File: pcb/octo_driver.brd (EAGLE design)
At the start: 34.3 x 46.2 mm, 22 parts, among them U1 LP2985-10DBVT

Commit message: fixed lots of warnings, general cleanup
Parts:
- removed TP1: PTR1B2,54, testpad:B2,54
- C3: value (none) -> 1uF
- JP1, SV1: value (none) -> (none)
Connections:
- new net N$2: C1.1, U1.5
- net GND: now also H2.B2,8, H3.B2,8; no longer TP1.TP
- net VCC: no longer C1.1, U1.5
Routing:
- net VCC: track 68.4 -> 64.6 mm
- net N$2: track 0.00 -> 2.25 mm
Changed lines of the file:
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@@
 <attribute name="NAME" x="59.182" y="46.355" size="1.27" layer="25" rot="R270"/>
 </element>
-<element name="JP1" library="SparkFun-Connectors" package="1X02" value="" x="39.878" y="66.548" smashed="yes" rot="R270">
+<element name="JP1" library="SparkFun-Connectors" package="1X02" value=" " x="39.878" y="66.548" smashed="yes" rot="R270">
 <attribute name="VALUE" x="36.703" y="67.818" size="1.27" layer="27" rot="R270"/>
 </element>
@@
 <element name="H2" library="holes" package="2,8-PAD" value="MOUNT-PAD-ROUND2.8" x="40.666" y="71.12"/>
 <element name="H3" library="holes" package="2,8-PAD" value="MOUNT-PAD-ROUND2.8" x="66.294" y="71.12"/>
-<element name="C3" library="rcl" package="C0805" value="" x="55.88" y="33.782" smashed="yes">
-<attribute name="NAME" x="58.166" y="33.274" size="1.27" layer="25"/>
-<attribute name="VALUE" x="54.61" y="31.242" size="1.27" layer="27"/>
-</element>
-<element name="SV1" library="penrose-con-lstb" package="MA09-1" value="" x="39.878" y="50.546" smashed="yes" rot="R90">
+<element name="C3" library="rcl" package="C0805" value="1uF" x="55.88" y="33.782" smashed="yes">
+<attribute name="VALUE" x="57.658" y="33.274" size="1.27" layer="27"/>
+</element>
+<element name="SV1" library="penrose-con-lstb" package="MA09-1" value=" " x="39.878" y="50.546" smashed="yes" rot="R90">
 <attribute name="OC_NEWARK" value="unknown" x="39.878" y="50.546" size="1.778" layer="27" rot="R90" display="off"/>
 <attribute name="MPN" value="" x="39.878" y="50.546" size="1.778" layer="27" rot="R90" display="off"/>
@@
 <element name="C2" library="rcl" package="C0805" value="1uF" x="43.18" y="66.548" smashed="yes">
 <attribute name="NAME" x="41.91" y="67.818" size="1.27" layer="25" font="vector" ratio="20" display="off"/>
-<attribute name="VALUE" x="41.91" y="64.008" size="1.016" layer="25" font="vector" ratio="20"/>
+<attribute name="VALUE" x="41.656" y="64.262" size="1.016" layer="25" font="vector" ratio="20"/>
 </element>
 <element name="U$1" library="penrose" package="PENROSELOGO_LOWDPI" value="" x="59.436" y="69.85"/>
 <element name="U$2" library="penrose" package="PENROSELOGO_1.75IN" value="" x="44.196" y="49.276"/>
-<element name="TP1" library="testpad" package="B2,54" value="PTR1B2,54" x="46.228" y="31.496">
-<attribute name="TP_SIGNAL_NAME" value="" x="46.228" y="31.496" size="1.778" layer="27" display="off"/>
-</element>
 </elements>
 <signals>
@@
 </polygon>
 <contactref element="C3" pad="2"/>
-<contactref element="H1" pad="B2,8"/>
 <contactref element="U1" pad="2"/>
 <contactref element="C2" pad="1"/>
 <contactref element="C1" pad="2"/>
-<contactref element="TP1" pad="TP"/>
+<contactref element="H3" pad="B2,8"/>
+<contactref element="H1" pad="B2,8"/>
+<contactref element="H2" pad="B2,8"/>
 </signal>
 <signal name="N$16">
@@
 <wire x1="54.93" y1="35.372" x2="56.134" y2="36.576" width="0.6096" layer="1"/>
 <wire x1="63.754" y1="36.576" x2="56.134" y2="36.576" width="0.6096" layer="1"/>
-<contactref element="U1" pad="5"/>
-<contactref element="C1" pad="1"/>
-<wire x1="48.7934" y1="64.6938" x2="48.7934" y2="66.4566" width="0.4064" layer="1"/>
-<wire x1="48.7934" y1="66.4566" x2="48.448" y2="66.802" width="0.4064" layer="1"/>
-<wire x1="48.7934" y1="64.6938" x2="49.784" y2="65.9638" width="0.6096" layer="1"/>
 <wire x1="49.784" y1="65.9638" x2="66.548" y2="66.04" width="0.6096" layer="1"/>
 <wire x1="66.548" y1="66.04" x2="67.564" y2="65.532" width="0.6096" layer="1"/>
@@
 <wire x1="54.93" y1="35.372" x2="54.864" y2="35.306" width="0" layer="19" extent="1-1"/>
 </signal>
+<signal name="N$2">
+<contactref element="U1" pad="5"/>
+<contactref element="C1" pad="1"/>
+<wire x1="48.7934" y1="64.6938" x2="48.7934" y2="66.4566" width="0.4064" layer="1"/>
+<wire x1="48.7934" y1="66.4566" x2="48.448" y2="66.802" width="0.4064" layer="1"/>
+</signal>
 </signals>

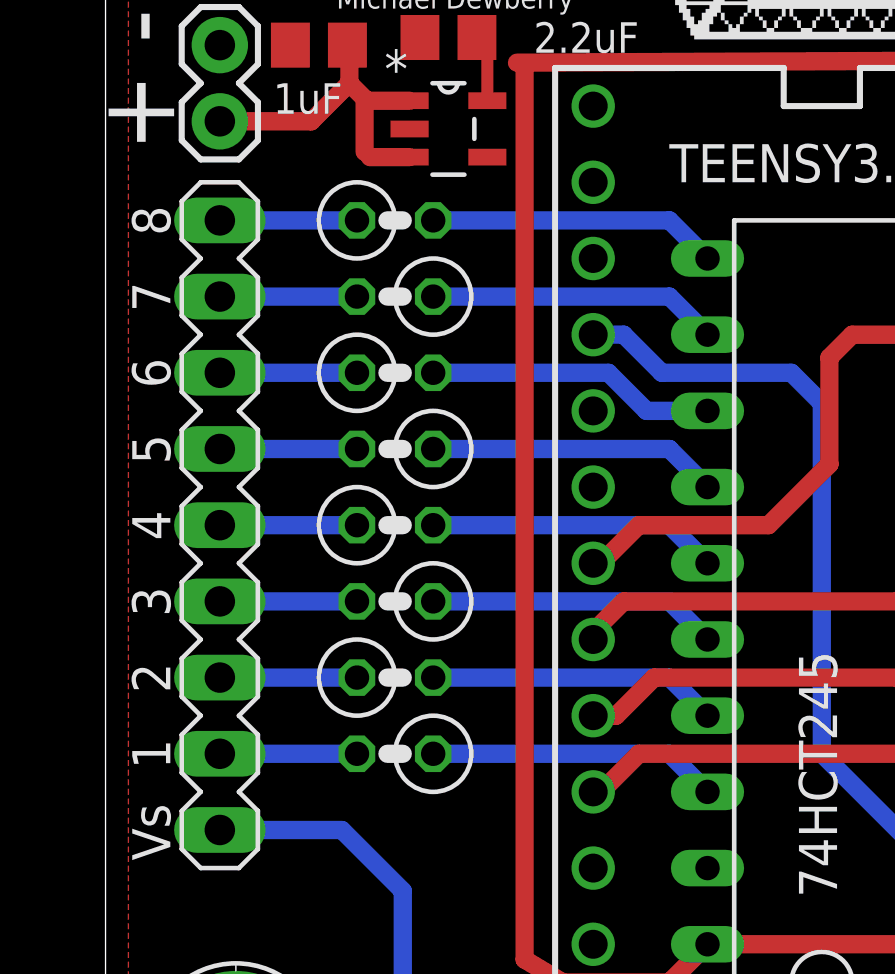
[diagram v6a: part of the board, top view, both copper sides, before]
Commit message: switched resistors to 0805 smt
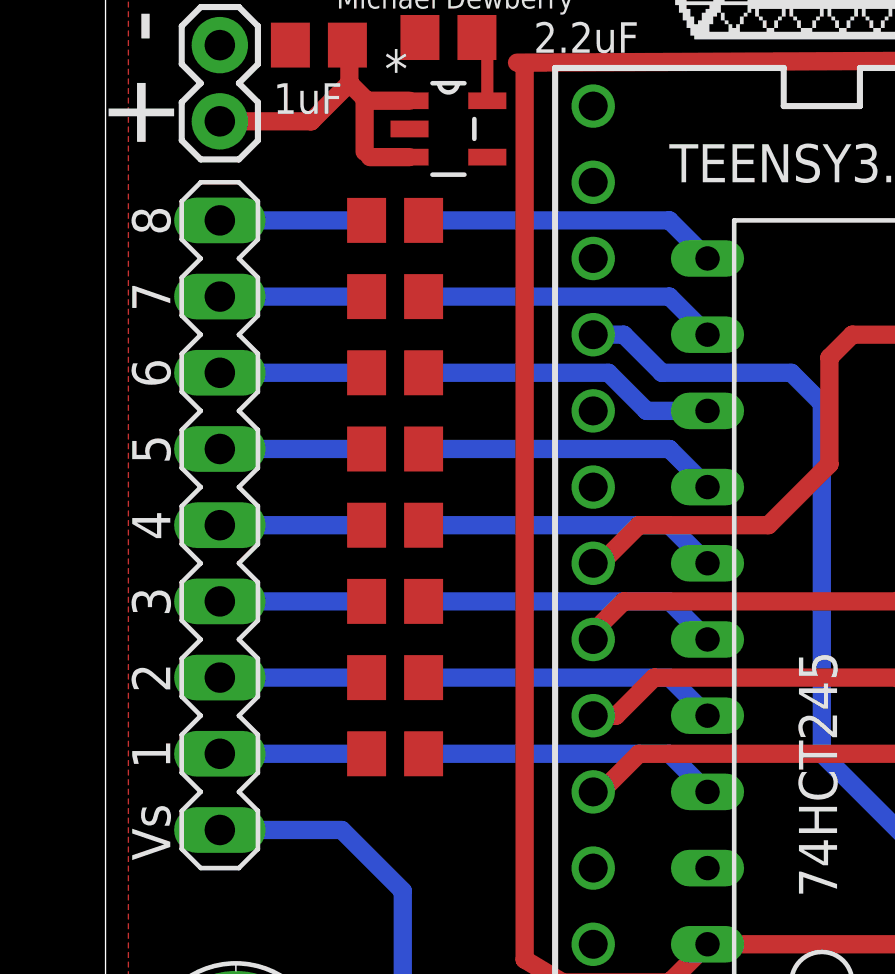
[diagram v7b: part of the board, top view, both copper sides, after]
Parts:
- RLED1, RLED10, RLED11, RLED12, RLED13, RLED14, RLED8, RLED9: device rcl:0207/2V -> rcl:R0805
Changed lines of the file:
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@@
 <attribute name="VALUE" x="36.703" y="67.818" size="1.27" layer="27" rot="R270"/>
 </element>
-<element name="RLED1" library="rcl" package="0207/2V" value="220" x="45.72" y="60.706" smashed="yes">
+<element name="RLED1" library="rcl" package="R0805" value="220" x="45.72" y="60.706" smashed="yes">
 <attribute name="NAME" x="45.6692" y="61.722" size="1.27" layer="25" ratio="10" display="off"/>
 <attribute name="VALUE" x="45.6692" y="58.4708" size="1.27" layer="27" ratio="10" display="off"/>
 </element>
-<element name="RLED8" library="rcl" package="0207/2V" value="220" x="45.72" y="58.166" smashed="yes" rot="R180">
+<element name="RLED8" library="rcl" package="R0805" value="220" x="45.72" y="58.166" smashed="yes" rot="R180">
 <attribute name="NAME" x="45.7708" y="57.15" size="1.27" layer="25" ratio="10" rot="R180" display="off"/>
 <attribute name="VALUE" x="45.7708" y="60.4012" size="1.27" layer="27" ratio="10" rot="R180" display="off"/>
 </element>
-<element name="RLED9" library="rcl" package="0207/2V" value="220" x="45.72" y="55.626" smashed="yes">
+<element name="RLED9" library="rcl" package="R0805" value="220" x="45.72" y="55.626" smashed="yes">
 <attribute name="NAME" x="45.6692" y="56.642" size="1.27" layer="25" ratio="10" display="off"/>
 <attribute name="VALUE" x="45.6692" y="53.3908" size="1.27" layer="27" ratio="10" display="off"/>
 </element>
-<element name="RLED10" library="rcl" package="0207/2V" value="220" x="45.72" y="53.086" smashed="yes" rot="R180">
+<element name="RLED10" library="rcl" package="R0805" value="220" x="45.72" y="53.086" smashed="yes" rot="R180">
 <attribute name="NAME" x="45.7708" y="52.07" size="1.27" layer="25" ratio="10" rot="R180" display="off"/>
 <attribute name="VALUE" x="45.7708" y="55.3212" size="1.27" layer="27" ratio="10" rot="R180" display="off"/>
 </element>
-<element name="RLED11" library="rcl" package="0207/2V" value="220" x="45.72" y="50.546" smashed="yes">
+<element name="RLED11" library="rcl" package="R0805" value="220" x="45.72" y="50.546" smashed="yes">
 <attribute name="NAME" x="45.6692" y="51.562" size="1.27" layer="25" ratio="10" display="off"/>
 <attribute name="VALUE" x="45.6692" y="48.3108" size="1.27" layer="27" ratio="10" display="off"/>
 </element>
-<element name="RLED12" library="rcl" package="0207/2V" value="220" x="45.72" y="48.006" smashed="yes" rot="R180">
+<element name="RLED12" library="rcl" package="R0805" value="220" x="45.72" y="48.006" smashed="yes" rot="R180">
 <attribute name="NAME" x="45.7708" y="46.99" size="1.27" layer="25" ratio="10" rot="R180" display="off"/>
 <attribute name="VALUE" x="45.7708" y="50.2412" size="1.27" layer="27" ratio="10" rot="R180" display="off"/>
 </element>
-<element name="RLED13" library="rcl" package="0207/2V" value="220" x="45.72" y="45.466" smashed="yes">
+<element name="RLED13" library="rcl" package="R0805" value="220" x="45.72" y="45.466" smashed="yes">
 <attribute name="NAME" x="45.6692" y="46.482" size="1.27" layer="25" ratio="10" display="off"/>
 <attribute name="VALUE" x="45.6692" y="43.2308" size="1.27" layer="27" ratio="10" display="off"/>
 </element>
-<element name="RLED14" library="rcl" package="0207/2V" value="220" x="45.72" y="42.926" smashed="yes" rot="R180">
+<element name="RLED14" library="rcl" package="R0805" value="220" x="45.72" y="42.926" smashed="yes" rot="R180">
 <attribute name="NAME" x="45.7708" y="41.91" size="1.27" layer="25" ratio="10" rot="R180" display="off"/>
 <attribute name="VALUE" x="45.7708" y="45.1612" size="1.27" layer="27" ratio="10" rot="R180" display="off"/>
@@
 <contactref element="RLED1" pad="2"/>
 <contactref element="74HCT245" pad="11"/>
-<wire x1="46.99" y1="60.706" x2="54.864" y2="60.706" width="0.6096" layer="16"/>
+<wire x1="46.67" y1="60.706" x2="54.864" y2="60.706" width="0.6096" layer="16"/>
 <wire x1="54.864" y1="60.706" x2="56.134" y2="59.436" width="0.6096" layer="16"/>
 </signal>
@@
 <contactref element="74HCT245" pad="12"/>
 <contactref element="RLED8" pad="1"/>
-<wire x1="46.99" y1="58.166" x2="54.864" y2="58.166" width="0.6096" layer="16"/>
+<wire x1="46.67" y1="58.166" x2="54.864" y2="58.166" width="0.6096" layer="16"/>
 <wire x1="54.864" y1="58.166" x2="56.134" y2="56.896" width="0.6096" layer="16"/>
 </signal>
@@
 <contactref element="RLED9" pad="2"/>
 <contactref element="74HCT245" pad="13"/>
-<wire x1="46.99" y1="55.626" x2="52.832" y2="55.626" width="0.6096" layer="16"/>
+<wire x1="46.67" y1="55.626" x2="52.832" y2="55.626" width="0.6096" layer="16"/>
 <wire x1="52.832" y1="55.626" x2="54.102" y2="54.356" width="0.6096" layer="16"/>
 <wire x1="54.102" y1="54.356" x2="56.134" y2="54.356" width="0.6096" layer="16"/>
@@
 <contactref element="74HCT245" pad="14"/>
 <contactref element="RLED10" pad="1"/>
-<wire x1="46.99" y1="53.086" x2="54.864" y2="53.086" width="0.6096" layer="16"/>
+<wire x1="46.67" y1="53.086" x2="54.864" y2="53.086" width="0.6096" layer="16"/>
 <wire x1="54.864" y1="53.086" x2="56.134" y2="51.816" width="0.6096" layer="16"/>
 </signal>
@@
 <contactref element="RLED11" pad="2"/>
 <contactref element="74HCT245" pad="15"/>
-<wire x1="46.99" y1="50.546" x2="54.864" y2="50.546" width="0.6096" layer="16"/>
+<wire x1="46.67" y1="50.546" x2="54.864" y2="50.546" width="0.6096" layer="16"/>
 <wire x1="54.864" y1="50.546" x2="56.134" y2="49.276" width="0.6096" layer="16"/>
 </signal>
@@
 <contactref element="74HCT245" pad="16"/>
 <contactref element="RLED12" pad="1"/>
-<wire x1="46.99" y1="48.006" x2="54.864" y2="48.006" width="0.6096" layer="16"/>
+<wire x1="46.67" y1="48.006" x2="54.864" y2="48.006" width="0.6096" layer="16"/>
 <wire x1="54.864" y1="48.006" x2="56.134" y2="46.736" width="0.6096" layer="16"/>
 </signal>
@@
 <contactref element="RLED13" pad="2"/>
 <contactref element="74HCT245" pad="17"/>
-<wire x1="46.99" y1="45.466" x2="54.864" y2="45.466" width="0.6096" layer="16"/>
+<wire x1="46.67" y1="45.466" x2="54.864" y2="45.466" width="0.6096" layer="16"/>
 <wire x1="54.864" y1="45.466" x2="56.134" y2="44.196" width="0.6096" layer="16"/>
 </signal>
@@
 <contactref element="74HCT245" pad="18"/>
 <contactref element="RLED14" pad="1"/>
-<wire x1="46.99" y1="42.926" x2="54.864" y2="42.926" width="0.6096" layer="16"/>
+<wire x1="46.67" y1="42.926" x2="54.864" y2="42.926" width="0.6096" layer="16"/>
 <wire x1="54.864" y1="42.926" x2="56.134" y2="41.656" width="0.6096" layer="16"/>
 </signal>
@@
 <contactref element="RLED14" pad="2"/>
 <contactref element="SV1" pad="2"/>
-<wire x1="44.45" y1="42.926" x2="39.878" y2="42.926" width="0.6096" layer="16"/>
+<wire x1="44.77" y1="42.926" x2="39.878" y2="42.926" width="0.6096" layer="16"/>
 </signal>
 <signal name="LED2_3.3">
@@
 <contactref element="RLED13" pad="1"/>
 <contactref element="SV1" pad="3"/>
-<wire x1="39.878" y1="45.466" x2="44.45" y2="45.466" width="0.6096" layer="16"/>
+<wire x1="39.878" y1="45.466" x2="44.77" y2="45.466" width="0.6096" layer="16"/>
 </signal>
 <signal name="LED3">
 <contactref element="RLED12" pad="2"/>
 <contactref element="SV1" pad="4"/>
-<wire x1="44.45" y1="48.006" x2="39.878" y2="48.006" width="0.6096" layer="16"/>
+<wire x1="44.77" y1="48.006" x2="39.878" y2="48.006" width="0.6096" layer="16"/>
 </signal>
 <signal name="LED4">
 <contactref element="RLED11" pad="1"/>
 <contactref element="SV1" pad="5"/>
-<wire x1="39.878" y1="50.546" x2="44.45" y2="50.546" width="0.6096" layer="16"/>
+<wire x1="39.878" y1="50.546" x2="44.77" y2="50.546" width="0.6096" layer="16"/>
 </signal>
 <signal name="LED5">
 <contactref element="RLED10" pad="2"/>
 <contactref element="SV1" pad="6"/>
-<wire x1="44.45" y1="53.086" x2="39.878" y2="53.086" width="0.6096" layer="16"/>
+<wire x1="44.77" y1="53.086" x2="39.878" y2="53.086" width="0.6096" layer="16"/>
 </signal>
 <signal name="LED6">
 <contactref element="RLED9" pad="1"/>
 <contactref element="SV1" pad="7"/>
-<wire x1="39.878" y1="55.626" x2="44.45" y2="55.626" width="0.6096" layer="16"/>
+<wire x1="39.878" y1="55.626" x2="44.77" y2="55.626" width="0.6096" layer="16"/>
 </signal>
 <signal name="LED7">
 <contactref element="RLED8" pad="2"/>
 <contactref element="SV1" pad="8"/>
-<wire x1="44.45" y1="58.166" x2="39.878" y2="58.166" width="0.6096" layer="16"/>
+<wire x1="44.77" y1="58.166" x2="39.878" y2="58.166" width="0.6096" layer="16"/>
 </signal>
 <signal name="LED8">
 <contactref element="RLED1" pad="1"/>
 <contactref element="SV1" pad="9"/>
-<wire x1="39.878" y1="60.706" x2="44.45" y2="60.706" width="0.6096" layer="16"/>
+<wire x1="39.878" y1="60.706" x2="44.77" y2="60.706" width="0.6096" layer="16"/>
 </signal>
 <signal name="LED1_3.3">
